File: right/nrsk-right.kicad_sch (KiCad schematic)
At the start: 119 parts, among them J1 PJ-320D, J2 USB-C, SW1 71, SW10 8, SW11 9, SW12 0, SW13 -, SW14 =, SW15 Backspace, SW16 75, SW17 Y, SW18 U, SW19 I, SW2 F7, SW20 O, SW21 P, SW22 [, SW23 ], SW24 \, SW25 77, SW26 H, SW27 J, SW28 K, SW29 L, SW3 F8, SW30 ;, SW31 ', SW32 Enter, SW33 79, SW34 N, SW35 M, SW36 ,, SW37 ., SW38 /, SW39 ↑, SW4 F9, SW40 fn, SW41 81, SW42 Space, SW43 Space, SW44 Cmd, SW45 Opt, SW46 ←, SW47 ↓, SW48 →, SW5 F10, SW6 F11, SW7 F12, SW8 73, SW9 7, U1 ATmega32U4-AU, U2 USBLC6-2SC6, Y1 16MHz

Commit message: Add OLED displays, OLED placement study and high-resolution renders
- 0.91" 128x32 SSD1306 OLED on both halves (I2C on PD0/PD1, 4.7k pull-ups),
  placed in the key-free inner notch; boards re-routed, ERC/DRC clean
- Switch plate window with a 2 mm clear acrylic cover lying on the plate,
  shaped around the switch tops; keyboard height unchanged
- QMK: OLED enabled (layer/caps on the master, WPM on the other half),
  split sync of layer, LED state and WPM
- BOM: OLED modules, pull-ups, cover acrylic and screws
- OLED height/tilt study: flush, 3.5/6.5/13 mm pods and two tilted pods,
  checked clear of keycaps and inside the case outline
- Blender renders at 2400 px and a grouped, numbered overview sheet

Co-Authored-By: Claude Opus 5.5 <noreply@anthropic.com>
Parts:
- added J3: OLED 128x32, nrsk:OLED_0.91in_128x32_I2C, symbol Connector_Generic:Conn_01x04
- added R8, R9: 4.7k, Resistor_SMD:R_0805_2012Metric, symbol Device:R
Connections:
- net GND: now also J3.1 (Pin_1)
- net VCC: now also J3.2 (Pin_2), R8.1, R9.1
- net SCL: now reaches U1.18 (PD0)
- net SCL: now also J3.3 (Pin_3), R8.2
- net SDA: now reaches U1.19 (PD1)
- net SDA: now also J3.4 (Pin_4), R9.2
- no-connect marks 13 -> 11
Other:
- note added: "OLED 0.91" 128x32 (I2C, SSD1306)"
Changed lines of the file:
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@@
 	(label "XTAL2" (at 264.16 88.90 180) (effects (font (size 1.27 1.27)) (justify right bottom)))
 	(label "XTAL1" (at 264.16 83.82 180) (effects (font (size 1.27 1.27)) (justify right bottom)))
-	(no_connect (at 294.64 109.22))
-	(no_connect (at 294.64 111.76))
+	(label "SCL" (at 294.64 109.22 0) (effects (font (size 1.27 1.27)) (justify left bottom)))
+	(label "SDA" (at 294.64 111.76 0) (effects (font (size 1.27 1.27)) (justify left bottom)))
 	(label "DATA" (at 294.64 114.30 0) (effects (font (size 1.27 1.27)) (justify left bottom)))
 	(label "HAND" (at 294.64 116.84 0) (effects (font (size 1.27 1.27)) (justify left bottom)))
@@
 	)
 	(label "DATA" (at 347.98 180.34 0) (effects (font (size 1.27 1.27)) (justify left bottom)))
+	(text "OLED 0.91\" 128x32 (I2C, SSD1306)" (exclude_from_sim no) (at 330.20 200.66 0) (effects (font (size 2.0 2.0) (bold yes)) (justify left bottom)))
+	(symbol (lib_id "Connector_Generic:Conn_01x04") (at 342.90 215.90 0) (unit 1) (exclude_from_sim no) (in_bom yes) (on_board yes) (dnp no)
+	  (property "Reference" "J3" (at 345.44 213.36 0) (effects (font (size 1.27 1.27)) (justify left)))
+	  (property "Value" "OLED 128x32" (at 345.44 218.44 0) (effects (font (size 1.27 1.27)) (justify left)))
+	  (property "Footprint" "nrsk:OLED_0.91in_128x32_I2C" (at 342.90 215.90 0) (effects (font (size 1.27 1.27)) (hide yes)))
+	  (property "Datasheet" "" (at 342.90 215.90 0) (effects (font (size 1.27 1.27)) (hide yes)))
+	  (pin "1")
+	  (pin "2")
+	  (pin "3")
+	  (pin "4")
+	  (instances (project "nrsk-right" (path "/ed20d8a8-6cf2-52f9-90d9-bd3277b2df44" (reference "J3") (unit 1))))
+	)
+	(wire (pts (xy 337.82 213.36) (xy 332.74 213.36)) (stroke (width 0) (type default)))
+	(symbol (lib_id "power:GND") (at 332.74 213.36 270) (unit 1) (exclude_from_sim no) (in_bom no) (on_board no) (dnp no)
+	  (property "Reference" "#PWR037" (at 332.74 213.36 0) (effects (font (size 1.27 1.27)) (justify left) (hide yes)))
+	  (property "Value" "GND" (at 332.74 217.17 0) (effects (font (size 1.27 1.27)) (justify left)))
+	  (property "Footprint" "" (at 332.74 213.36 0) (effects (font (size 1.27 1.27)) (hide yes)))
+	  (property "Datasheet" "" (at 332.74 213.36 0) (effects (font (size 1.27 1.27)) (hide yes)))
+	  (pin "1")
+	  (instances (project "nrsk-right" (path "/ed20d8a8-6cf2-52f9-90d9-bd3277b2df44" (reference "#PWR037") (unit 1))))
+	)
+	(wire (pts (xy 337.82 215.90) (xy 332.74 215.90)) (stroke (width 0) (type default)))
+	(symbol (lib_id "power:VCC") (at 332.74 215.90 90) (unit 1) (exclude_from_sim no) (in_bom no) (on_board no) (dnp no)
+	  (property "Reference" "#PWR038" (at 332.74 215.90 0) (effects (font (size 1.27 1.27)) (justify left) (hide yes)))
+	  (property "Value" "VCC" (at 332.74 212.09 0) (effects (font (size 1.27 1.27)) (justify left)))
+	  (property "Footprint" "" (at 332.74 215.90 0) (effects (font (size 1.27 1.27)) (hide yes)))
+	  (property "Datasheet" "" (at 332.74 215.90 0) (effects (font (size 1.27 1.27)) (hide yes)))
+	  (pin "1")
+	  (instances (project "nrsk-right" (path "/ed20d8a8-6cf2-52f9-90d9-bd3277b2df44" (reference "#PWR038") (unit 1))))
+	)
+	(label "SCL" (at 337.82 218.44 180) (effects (font (size 1.27 1.27)) (justify right bottom)))
+	(label "SDA" (at 337.82 220.98 180) (effects (font (size 1.27 1.27)) (justify right bottom)))
+	(symbol (lib_id "Device:R") (at 368.30 213.36 0) (unit 1) (exclude_from_sim no) (in_bom yes) (on_board yes) (dnp no)
+	  (property "Reference" "R8" (at 370.84 210.82 0) (effects (font (size 1.27 1.27)) (justify left)))
+	  (property "Value" "4.7k" (at 370.84 215.90 0) (effects (font (size 1.27 1.27)) (justify left)))
+	  (property "Footprint" "Resistor_SMD:R_0805_2012Metric" (at 368.30 213.36 0) (effects (font (size 1.27 1.27)) (hide yes)))
+	  (property "Datasheet" "" (at 368.30 213.36 0) (effects (font (size 1.27 1.27)) (hide yes)))
+	  (pin "1")
+	  (pin "2")
+	  (instances (project "nrsk-right" (path "/ed20d8a8-6cf2-52f9-90d9-bd3277b2df44" (reference "R8") (unit 1))))
+	)
+	(wire (pts (xy 368.30 209.55) (xy 368.30 204.47)) (stroke (width 0) (type default)))
+	(symbol (lib_id "power:VCC") (at 368.30 204.47 0) (unit 1) (exclude_from_sim no) (in_bom no) (on_board no) (dnp no)
+	  (property "Reference" "#PWR039" (at 368.30 204.47 0) (effects (font (size 1.27 1.27)) (justify left) (hide yes)))
+	  (property "Value" "VCC" (at 368.30 200.66 0) (effects (font (size 1.27 1.27)) (justify left)))
+	  (property "Footprint" "" (at 368.30 204.47 0) (effects (font (size 1.27 1.27)) (hide yes)))
+	  (property "Datasheet" "" (at 368.30 204.47 0) (effects (font (size 1.27 1.27)) (hide yes)))
+	  (pin "1")
+	  (instances (project "nrsk-right" (path "/ed20d8a8-6cf2-52f9-90d9-bd3277b2df44" (reference "#PWR039") (unit 1))))
+	)
+	(label "SCL" (at 368.30 217.17 270) (effects (font (size 1.27 1.27)) (justify right bottom)))
+	(symbol (lib_id "Device:R") (at 378.46 213.36 0) (unit 1) (exclude_from_sim no) (in_bom yes) (on_board yes) (dnp no)
+	  (property "Reference" "R9" (at 381.00 210.82 0) (effects (font (size 1.27 1.27)) (justify left)))
+	  (property "Value" "4.7k" (at 381.00 215.90 0) (effects (font (size 1.27 1.27)) (justify left)))
+	  (property "Footprint" "Resistor_SMD:R_0805_2012Metric" (at 378.46 213.36 0) (effects (font (size 1.27 1.27)) (hide yes)))
+	  (property "Datasheet" "" (at 378.46 213.36 0) (effects (font (size 1.27 1.27)) (hide yes)))
+	  (pin "1")
+	  (pin "2")
+	  (instances (project "nrsk-right" (path "/ed20d8a8-6cf2-52f9-90d9-bd3277b2df44" (reference "R9") (unit 1))))
+	)
+	(wire (pts (xy 378.46 209.55) (xy 378.46 204.47)) (stroke (width 0) (type default)))
+	(symbol (lib_id "power:VCC") (at 378.46 204.47 0) (unit 1) (exclude_from_sim no) (in_bom no) (on_board no) (dnp no)
+	  (property "Reference" "#PWR040" (at 378.46 204.47 0) (effects (font (size 1.27 1.27)) (justify left) (hide yes)))
+	  (property "Value" "VCC" (at 378.46 200.66 0) (effects (font (size 1.27 1.27)) (justify left)))
+	  (property "Footprint" "" (at 378.46 204.47 0) (effects (font (size 1.27 1.27)) (hide yes)))
+	  (property "Datasheet" "" (at 378.46 204.47 0) (effects (font (size 1.27 1.27)) (hide yes)))
+	  (pin "1")
+	  (instances (project "nrsk-right" (path "/ed20d8a8-6cf2-52f9-90d9-bd3277b2df44" (reference "#PWR040") (unit 1))))
+	)
+	(label "SDA" (at 378.46 217.17 270) (effects (font (size 1.27 1.27)) (justify right bottom)))
 	(sheet_instances (path "/" (page "1")))
 	(embedded_fonts no)

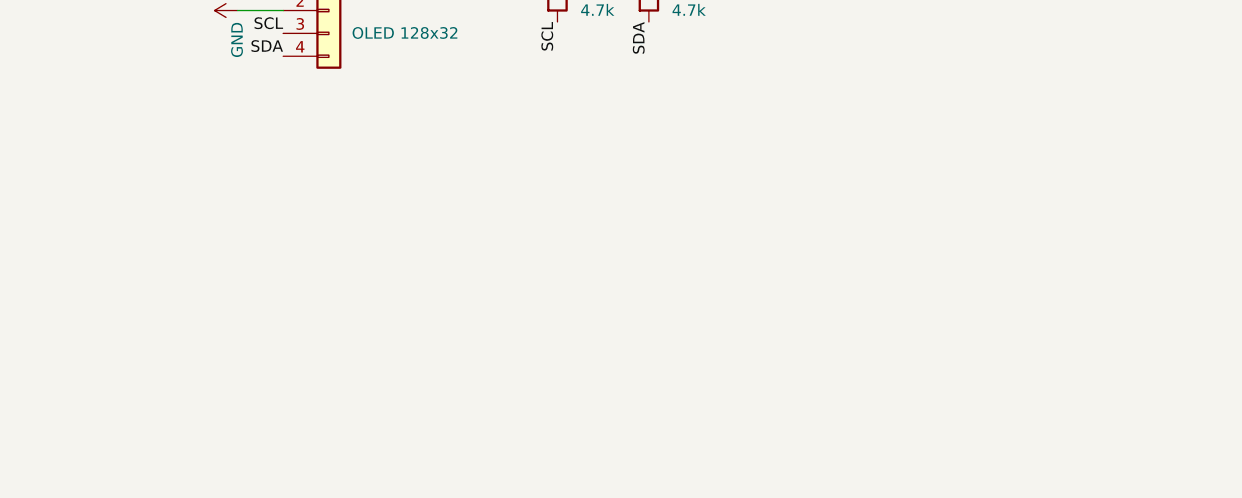
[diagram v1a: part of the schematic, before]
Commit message: Add corner thumbwheels read by AS5600, preview-quality renders
- Thumbwheel (29.2 mm, knurled) at the left half's top-left and the right
  half's top-right corner, lying under the PCB with its rim out of the
  corner; read contact-free by an AS5600 on the PCB back through a
  diametric magnet, on the existing I2C bus (no extra pins)
- Left Esc switch turned 180 deg so its socket clears the sensor
- Case: wall opening at the corner, axle post (print) / M3 axle (acrylic),
  corner screws moved beside the opening, printable wheel STL
- QMK: nrsk.c polls the sensor and forwards the other half's steps over a
  split RPC; dial_update_user() in the keymap (volume / page by default)
- Router cleanup runs in a separate process (reloading a board in the
  same process returned a broken object and stopped the build)
- Renders default to a quick preview (1200 px); FINAL=1 for 2400 px
- Side dial comparison renders kept in docs/img/dial-study

Co-Authored-By: Claude Opus 5.5 <noreply@anthropic.com>
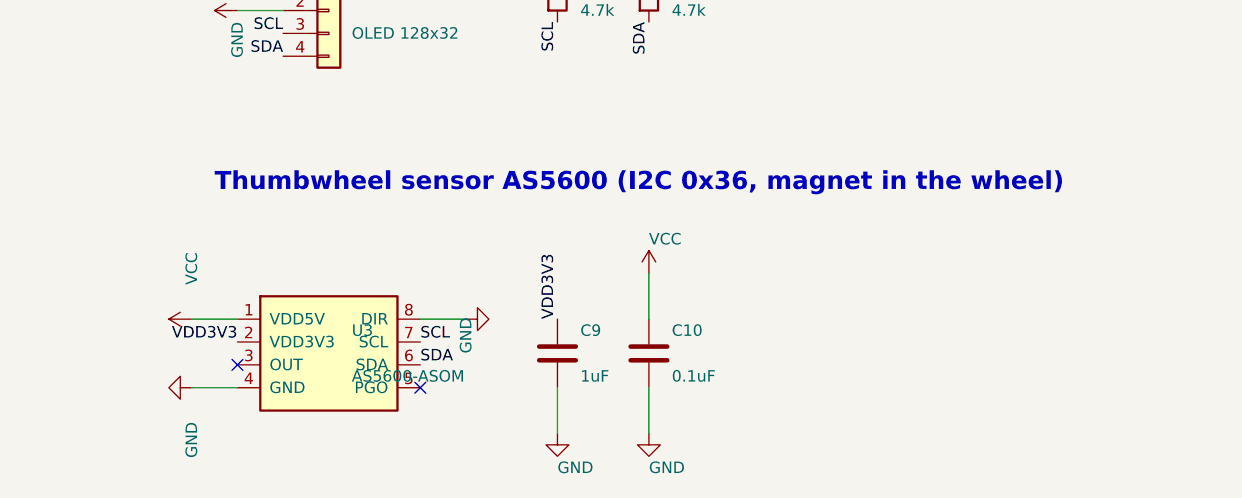
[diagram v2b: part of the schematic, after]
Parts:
- added C10: 0.1uF, Capacitor_SMD:C_0805_2012Metric, symbol Device:C
- added C9: 1uF, Capacitor_SMD:C_0805_2012Metric, symbol Device:C
- added U3: AS5600-ASOM, Package_SO:SOIC-8_3.9x4.9mm_P1.27mm, symbol nrsk:AS5600
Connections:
- net GND: now also C10.2, C9.2, U3.4 (GND), U3.8 (DIR)
- net SCL: now also U3.7 (SCL)
- net SDA: now also U3.6 (SDA)
- net VCC: now also C10.1, U3.1 (VDD5V)
- new net VDD3V3: C9.1, U3.2 (VDD3V3)
- no-connect marks 11 -> 13
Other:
- note added: "Thumbwheel sensor AS5600 (I2C 0x36, magnet in the wheel)"
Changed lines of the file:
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@@
 	)
 	(label "SDA" (at 378.46 217.17 270) (effects (font (size 1.27 1.27)) (justify right bottom)))
+	(text "Thumbwheel sensor AS5600 (I2C 0x36, magnet in the wheel)" (exclude_from_sim no) (at 330.20 236.22 0) (effects (font (size 2.0 2.0) (bold yes)) (justify left bottom)))
+	(symbol (lib_id "nrsk:AS5600") (at 342.90 254.00 0) (unit 1) (exclude_from_sim no) (in_bom yes) (on_board yes) (dnp no)
+	  (property "Reference" "U3" (at 345.44 251.46 0) (effects (font (size 1.27 1.27)) (justify left)))
+	  (property "Value" "AS5600-ASOM" (at 345.44 256.54 0) (effects (font (size 1.27 1.27)) (justify left)))
+	  (property "Footprint" "Package_SO:SOIC-8_3.9x4.9mm_P1.27mm" (at 342.90 254.00 0) (effects (font (size 1.27 1.27)) (hide yes)))
+	  (property "Datasheet" "" (at 342.90 254.00 0) (effects (font (size 1.27 1.27)) (hide yes)))
+	  (pin "1")
+	  (pin "2")
+	  (pin "3")
+	  (pin "4")
+	  (pin "5")
+	  (pin "6")
+	  (pin "7")
+	  (pin "8")
+	  (instances (project "nrsk-right" (path "/ed20d8a8-6cf2-52f9-90d9-bd3277b2df44" (reference "U3") (unit 1))))
+	)
+	(wire (pts (xy 332.74 250.19) (xy 327.66 250.19)) (stroke (width 0) (type default)))
+	(symbol (lib_id "power:VCC") (at 327.66 250.19 90) (unit 1) (exclude_from_sim no) (in_bom no) (on_board no) (dnp no)
+	  (property "Reference" "#PWR041" (at 327.66 250.19 0) (effects (font (size 1.27 1.27)) (justify left) (hide yes)))
+	  (property "Value" "VCC" (at 327.66 246.38 0) (effects (font (size 1.27 1.27)) (justify left)))
+	  (property "Footprint" "" (at 327.66 250.19 0) (effects (font (size 1.27 1.27)) (hide yes)))
+	  (property "Datasheet" "" (at 327.66 250.19 0) (effects (font (size 1.27 1.27)) (hide yes)))
+	  (pin "1")
+	  (instances (project "nrsk-right" (path "/ed20d8a8-6cf2-52f9-90d9-bd3277b2df44" (reference "#PWR041") (unit 1))))
+	)
+	(label "VDD3V3" (at 332.74 252.73 180) (effects (font (size 1.27 1.27)) (justify right bottom)))
+	(no_connect (at 332.74 255.27))
+	(wire (pts (xy 332.74 257.81) (xy 327.66 257.81)) (stroke (width 0) (type default)))
+	(symbol (lib_id "power:GND") (at 327.66 257.81 270) (unit 1) (exclude_from_sim no) (in_bom no) (on_board no) (dnp no)
+	  (property "Reference" "#PWR042" (at 327.66 257.81 0) (effects (font (size 1.27 1.27)) (justify left) (hide yes)))
+	  (property "Value" "GND" (at 327.66 261.62 0) (effects (font (size 1.27 1.27)) (justify left)))
+	  (property "Footprint" "" (at 327.66 257.81 0) (effects (font (size 1.27 1.27)) (hide yes)))
+	  (property "Datasheet" "" (at 327.66 257.81 0) (effects (font (size 1.27 1.27)) (hide yes)))
+	  (pin "1")
+	  (instances (project "nrsk-right" (path "/ed20d8a8-6cf2-52f9-90d9-bd3277b2df44" (reference "#PWR042") (unit 1))))
+	)
+	(no_connect (at 353.06 257.81))
+	(label "SDA" (at 353.06 255.27 0) (effects (font (size 1.27 1.27)) (justify left bottom)))
+	(label "SCL" (at 353.06 252.73 0) (effects (font (size 1.27 1.27)) (justify left bottom)))
+	(wire (pts (xy 353.06 250.19) (xy 358.14 250.19)) (stroke (width 0) (type default)))
+	(symbol (lib_id "power:GND") (at 358.14 250.19 90) (unit 1) (exclude_from_sim no) (in_bom no) (on_board no) (dnp no)
+	  (property "Reference" "#PWR043" (at 358.14 250.19 0) (effects (font (size 1.27 1.27)) (justify left) (hide yes)))
+	  (property "Value" "GND" (at 358.14 254.00 0) (effects (font (size 1.27 1.27)) (justify left)))
+	  (property "Footprint" "" (at 358.14 250.19 0) (effects (font (size 1.27 1.27)) (hide yes)))
+	  (property "Datasheet" "" (at 358.14 250.19 0) (effects (font (size 1.27 1.27)) (hide yes)))
+	  (pin "1")
+	  (instances (project "nrsk-right" (path "/ed20d8a8-6cf2-52f9-90d9-bd3277b2df44" (reference "#PWR043") (unit 1))))
+	)
+	(symbol (lib_id "Device:C") (at 368.30 254.00 0) (unit 1) (exclude_from_sim no) (in_bom yes) (on_board yes) (dnp no)
+	  (property "Reference" "C9" (at 370.84 251.46 0) (effects (font (size 1.27 1.27)) (justify left)))
+	  (property "Value" "1uF" (at 370.84 256.54 0) (effects (font (size 1.27 1.27)) (justify left)))
+	  (property "Footprint" "Capacitor_SMD:C_0805_2012Metric" (at 368.30 254.00 0) (effects (font (size 1.27 1.27)) (hide yes)))
+	  (property "Datasheet" "" (at 368.30 254.00 0) (effects (font (size 1.27 1.27)) (hide yes)))
+	  (pin "1")
+	  (pin "2")
+	  (instances (project "nrsk-right" (path "/ed20d8a8-6cf2-52f9-90d9-bd3277b2df44" (reference "C9") (unit 1))))
+	)
+	(label "VDD3V3" (at 368.30 250.19 90) (effects (font (size 1.27 1.27)) (justify left bottom)))
+	(wire (pts (xy 368.30 257.81) (xy 368.30 262.89)) (stroke (width 0) (type default)))
+	(symbol (lib_id "power:GND") (at 368.30 262.89 0) (unit 1) (exclude_from_sim no) (in_bom no) (on_board no) (dnp no)
+	  (property "Reference" "#PWR044" (at 368.30 262.89 0) (effects (font (size 1.27 1.27)) (justify left) (hide yes)))
+	  (property "Value" "GND" (at 368.30 266.70 0) (effects (font (size 1.27 1.27)) (justify left)))
+	  (property "Footprint" "" (at 368.30 262.89 0) (effects (font (size 1.27 1.27)) (hide yes)))
+	  (property "Datasheet" "" (at 368.30 262.89 0) (effects (font (size 1.27 1.27)) (hide yes)))
+	  (pin "1")
+	  (instances (project "nrsk-right" (path "/ed20d8a8-6cf2-52f9-90d9-bd3277b2df44" (reference "#PWR044") (unit 1))))
+	)
+	(symbol (lib_id "Device:C") (at 378.46 254.00 0) (unit 1) (exclude_from_sim no) (in_bom yes) (on_board yes) (dnp no)
+	  (property "Reference" "C10" (at 381.00 251.46 0) (effects (font (size 1.27 1.27)) (justify left)))
+	  (property "Value" "0.1uF" (at 381.00 256.54 0) (effects (font (size 1.27 1.27)) (justify left)))
+	  (property "Footprint" "Capacitor_SMD:C_0805_2012Metric" (at 378.46 254.00 0) (effects (font (size 1.27 1.27)) (hide yes)))
+	  (property "Datasheet" "" (at 378.46 254.00 0) (effects (font (size 1.27 1.27)) (hide yes)))
+	  (pin "1")
+	  (pin "2")
+	  (instances (project "nrsk-right" (path "/ed20d8a8-6cf2-52f9-90d9-bd3277b2df44" (reference "C10") (unit 1))))
+	)
+	(wire (pts (xy 378.46 250.19) (xy 378.46 245.11)) (stroke (width 0) (type default)))
+	(symbol (lib_id "power:VCC") (at 378.46 245.11 0) (unit 1) (exclude_from_sim no) (in_bom no) (on_board no) (dnp no)
+	  (property "Reference" "#PWR045" (at 378.46 245.11 0) (effects (font (size 1.27 1.27)) (justify left) (hide yes)))
+	  (property "Value" "VCC" (at 378.46 241.30 0) (effects (font (size 1.27 1.27)) (justify left)))
+	  (property "Footprint" "" (at 378.46 245.11 0) (effects (font (size 1.27 1.27)) (hide yes)))
+	  (property "Datasheet" "" (at 378.46 245.11 0) (effects (font (size 1.27 1.27)) (hide yes)))
+	  (pin "1")
+	  (instances (project "nrsk-right" (path "/ed20d8a8-6cf2-52f9-90d9-bd3277b2df44" (reference "#PWR045") (unit 1))))
+	)
+	(wire (pts (xy 378.46 257.81) (xy 378.46 262.89)) (stroke (width 0) (type default)))
+	(symbol (lib_id "power:GND") (at 378.46 262.89 0) (unit 1) (exclude_from_sim no) (in_bom no) (on_board no) (dnp no)
+	  (property "Reference" "#PWR046" (at 378.46 262.89 0) (effects (font (size 1.27 1.27)) (justify left) (hide yes)))
+	  (property "Value" "GND" (at 378.46 266.70 0) (effects (font (size 1.27 1.27)) (justify left)))
+	  (property "Footprint" "" (at 378.46 262.89 0) (effects (font (size 1.27 1.27)) (hide yes)))
+	  (property "Datasheet" "" (at 378.46 262.89 0) (effects (font (size 1.27 1.27)) (hide yes)))
+	  (pin "1")
+	  (instances (project "nrsk-right" (path "/ed20d8a8-6cf2-52f9-90d9-bd3277b2df44" (reference "#PWR046") (unit 1))))
+	)
 	(sheet_instances (path "/" (page "1")))
 	(embedded_fonts no)
